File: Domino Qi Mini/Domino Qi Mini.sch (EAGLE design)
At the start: 88 parts, among them J1 MH22-1, J2 MH22-1, M1 DOMINO, Q1 AP2302GN, Q2 2SC4081, SW1 IT-1100, SW2 IT-1100, SW3 IT-1100, U1 ATMEGA32U4-XUMU, U2 MP2162GQH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

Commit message: Domino Qi Mini: work in progress
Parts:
- added U$7: DOMINO_QI_LOGO, Domino:DOMINO_QI_LOGO
- S1: value USB_MR5-003A -> USB_MR5-001; device Domino:USB_MR5-003A -> Domino:USB_MR5-001
- SW1, SW2, SW3: value IT-1100 -> IT-1210; device Domino:IT-1100 -> Domino:IT-1210; PARTNO IT-1100 -> (none)
- U1: value ATMEGA32U4-XUMU -> ATMEGA32U4-XUAU/MU; device Domino:ATMEGA32U4-XUMU -> Domino:ATMEGA32U4-XUAU/MU
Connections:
- net !RESET: now also SW1.1; no longer SW1.2
- net D+: now also D1.P$2; no longer D1.P$3
- net D-: now also D1.P$3; no longer D1.P$2
- net GND: now also SW1.2; no longer SW1.1
- net PE: now also S1.M3
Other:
- note removed: "Domino Core"
- note removed: "Domino Pi"
- note removed: "Domino Qi"
- moved on the sheet: C1, C29, R23, U1

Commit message: Work in progress: changed for PCB antenna and removed Schottky diode on Domino Qi Mini, first Domino Qi draft
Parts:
- removed D2: MBRM130LT1G, Domino:MBRM130LT1G
- A1: value ACA-5036-A2-CC-S -> RF_ANT1; device Domino:ACA-5036-A2-CC-S -> Domino:RF_ANT1
- D3, D4, D5, D6: device Domino:LED_0603 -> Domino:LED_0402
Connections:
- removed net +VUSB: D2.A, L1.1
- net !RESET: now also J1.18; no longer J1.5
- net +5V: now also L1.1; no longer D2.C
- net 3V3: now also J1.13; no longer J1.10
- net ANT0_50R: now also A1.FEED; no longer A1.A
- net AREF: now also J1.2; no longer J1.21
- net D4: now also J1.16; no longer J1.7
- net D5: now also J1.15; no longer J1.8
- net D6: now also J1.14; no longer J1.9
- net GND: now also A1.GND, J1.12; no longer A1.GND@1, A1.GND@2, J1.11
- net GP6: now also J1.3; no longer J1.20
- net HANDSHAKE: now also J1.11; no longer J1.12
- net IO10: now also J1.8; no longer J1.15
- net IO11: now also J1.7; no longer J1.16
- net IO12: now also J1.6; no longer J1.17
- net IO13: now also J1.4; no longer J1.19
- net IO8: now also J1.10; no longer J1.13
- net IO9: now also J1.9; no longer J1.14
- net RXD1: now also J1.21; no longer J1.2
- net SCL: now also J1.17; no longer J1.6
- net SDA: now also J1.19; no longer J1.4
- net TXD1: now also J1.20; no longer J1.3
- net VIN: now also J1.5; no longer J1.18

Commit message: Work in progress on Domino Qi Mini board
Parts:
- removed C2: 10u, Domino:CAP_0805
- removed C3: 100n, Domino:CAP_0402
- removed D7, D8, D9: MBRM130LT1G, Domino:MBRM130LT1G
- removed F1: 0ZCG0110FF2C, Domino:0ZCG0110FF2C
- removed L1: BLM31PG601SN1L, Domino:FB_1206
- added C32: 100n, Domino:CAP_0402
- added C33: 4u7, Domino:CAP_0805
- added C34: 10n, Domino:CAP_0402
- added L3: BLM31PG601SN1L, Domino:FB_1206
- added R26: 100k, Domino:RES_0402
- added R27: 15k, Domino:RES_0402
- added R28: 0R, Domino:RES_0402
- added U6: MP65151DJ, Domino:MP65151DJ
- R1, R2: device GeMiNi:RES_0402 -> Domino:RES_0402
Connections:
- removed net 5V: D9.C, J2.19
- removed net VPROT: F1.1, L1.2
- new net !FLAG: R28.1, U6.!FLAG
- new net EN_USB: R26.1, R28.2, U6.EN
- new net ILIM: R27.1, U6.ILIM
- net +3V3: now also J1.13; no longer D8.A
- net +5V: now also J1.5, J2.19, U6.OUT; no longer D7.C, D9.A, L1.1
- net 3V3: no longer D8.C, J1.13
- net GND: now also C32.2, C33.2, C34.2, R27.2, U6.GND; no longer C2.2, C3.2
- net VBUS: now also C34.1, L3.2; no longer C2.1, C3.1, F1.2
- net VIN: now also C32.1, C33.1, L3.1, R26.2, U6.IN; no longer D7.A, J1.5
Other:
- note added: "© 2014-2015, The Domino Team All rights reserved."
- note removed: "PolyFuse"
- note removed: "© 2014, The Domino Team All rights reserved."
- moved on the sheet: A1, C11, C12, C16, C22, C23, C24, C25, C29, C30, C31, C9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

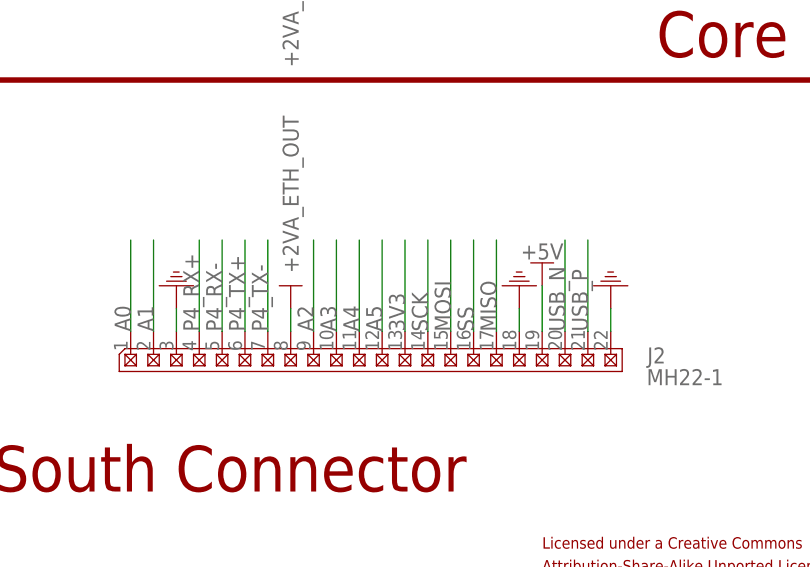
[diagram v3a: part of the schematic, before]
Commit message: Work in progress on Domino Qi Mini board: clustered all voltage translator chips instead of putting them close to ATMega32U4
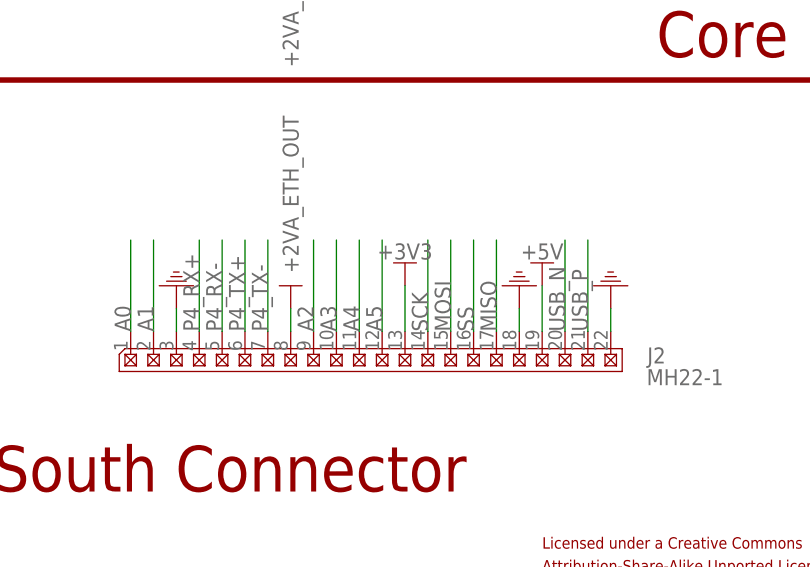
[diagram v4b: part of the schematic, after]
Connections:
- removed net 3V3: J2.13
- net +3V3: now also J2.13
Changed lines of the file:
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@@
 <?xml version="1.0" encoding="utf-8"?>
 <!DOCTYPE eagle SYSTEM "eagle.dtd">
-<eagle version="6.5.0">
+<eagle version="7.2.0">
 <drawing>
 <settings>
@@
 </part>
 <part name="SUPPLY56" library="Domino" deviceset="GND" device=""/>
+<part name="U$9" library="Domino" deviceset="+3V3" device=""/>
 </parts>
 <sheets>
@@
 </instance>
 <instance part="SUPPLY56" gate="GND" x="22.86" y="165.1" rot="MR0"/>
+<instance part="U$9" gate="G$1" x="287.02" y="50.8" smashed="yes" rot="MR0">
+<attribute name="VALUE" x="287.02" y="54.61" size="1.778" layer="96" rot="MR0" align="center"/>
+</instance>
 </instances>
 <busses>
@@
 <wire x1="284.48" y1="231.14" x2="284.48" y2="236.22" width="0.1524" layer="91"/>
 </segment>
+<segment>
+<wire x1="287.02" y1="45.72" x2="287.02" y2="50.8" width="0.1524" layer="91"/>
+<pinref part="J2" gate="G$1" pin="13"/>
+<pinref part="U$9" gate="G$1" pin="+3V3"/>
+</segment>
 </net>
 <net name="+3.3VD_IN" class="0">
@@
 </segment>
 </net>
-<net name="3V3" class="0">
-<segment>
-<wire x1="287.02" y1="45.72" x2="287.02" y2="55.88" width="0.1524" layer="91"/>
-<label x="287.02" y="45.72" size="1.778" layer="95" rot="R90"/>
-<pinref part="J2" gate="G$1" pin="13"/>
-</segment>
-</net>

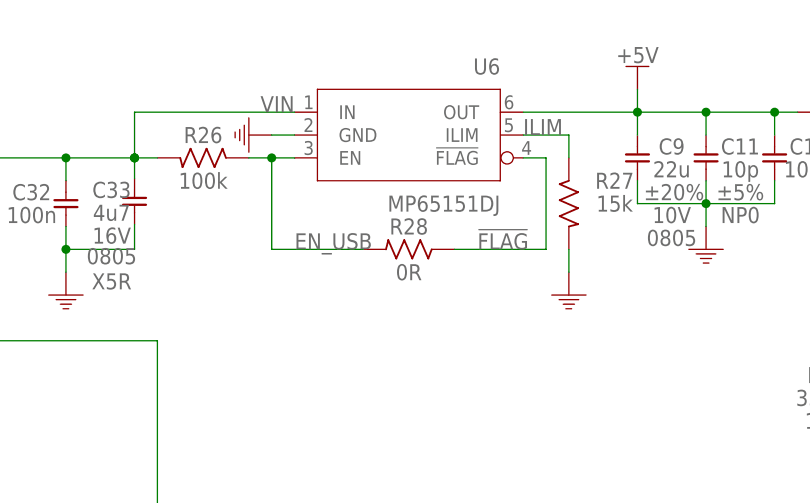
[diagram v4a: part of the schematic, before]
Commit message: Domino Qi Mini: only 1 airwire left!
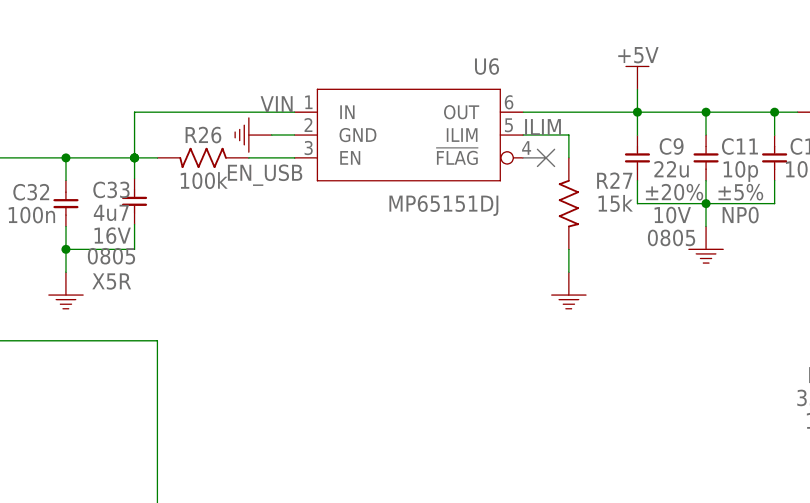
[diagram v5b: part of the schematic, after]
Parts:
- removed R28: 0R, Domino:RES_0402
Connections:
- removed net !FLAG: R28.1, U6.!FLAG
- net EN_USB: no longer R28.2
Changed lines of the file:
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@@
-<attribute name="TOL" value="5%"/>
-</part>
-<part name="R28" library="Domino" deviceset="RES_" device="0402" value="0R">
-<attribute name="PARTNO" value="R0402_0R_5%_62.5mW"/>
-<attribute name="RATE" value="62.5mW"/>
 <attribute name="TOL" value="5%"/>
 </part>
@@
 <part name="SUPPLY56" library="Domino" deviceset="GND" device=""/>
 <part name="U$9" library="Domino" deviceset="+3V3" device=""/>
+<part name="PORT3" library="Domino" deviceset="NC" device=""/>
 </parts>
 <sheets>
@@
 <attribute name="VALUE" x="73.66" y="236.22" size="1.778" layer="96" rot="MR0" align="center"/>
 </instance>
-<instance part="R28" gate="G$1" x="50.8" y="231.14" smashed="yes" rot="R180">
-<attribute name="PARTNO" x="50.8" y="231.14" size="1.778" layer="96" rot="R180" display="off"/>
-<attribute name="RATE" x="50.8" y="231.14" size="1.778" layer="96" rot="R180" display="off"/>
-<attribute name="SIZE" x="55.88" y="233.426" size="1.778" layer="96" align="center" display="off"/>
-<attribute name="TOL" x="50.8" y="231.14" size="1.778" layer="96" rot="R180" display="off"/>
-<attribute name="NAME" x="50.8" y="233.68" size="1.778" layer="95" rot="R180" align="center"/>
-<attribute name="VALUE" x="50.8" y="228.6" size="1.778" layer="96" rot="R180" align="center"/>
-</instance>
 <instance part="C34" gate="G$1" x="22.86" y="170.18" smashed="yes" rot="MR270">
 <attribute name="TC" x="22.86" y="170.18" size="1.778" layer="96" rot="MR270" display="off"/>
@@
 <attribute name="VALUE" x="287.02" y="54.61" size="1.778" layer="96" rot="MR0" align="center"/>
 </instance>
+<instance part="PORT3" gate="G$1" x="66.04" y="241.3" smashed="yes" rot="R180"/>
 </instances>
 <busses>
@@
 </segment>
 </net>
-<net name="!FLAG" class="0">
-<segment>
-<pinref part="R28" gate="G$1" pin="1"/>
-<wire x1="55.88" y1="231.14" x2="66.04" y2="231.14" width="0.1524" layer="91"/>
-<wire x1="66.04" y1="231.14" x2="66.04" y2="241.3" width="0.1524" layer="91"/>
-<pinref part="U6" gate="G$1" pin="!FLAG"/>
-<wire x1="66.04" y1="241.3" x2="63.5" y2="241.3" width="0.1524" layer="91"/>
-<label x="58.42" y="231.14" size="1.778" layer="95"/>
-</segment>
-</net>
 <net name="EN_USB" class="0">
 <segment>
-<wire x1="38.1" y1="241.3" x2="35.56" y2="241.3" width="0.1524" layer="91"/>
-<wire x1="35.56" y1="241.3" x2="33.02" y2="241.3" width="0.1524" layer="91"/>
+<label x="30.48" y="238.76" size="1.778" layer="95"/>
+<pinref part="U6" gate="G$1" pin="EN"/>
 <pinref part="R26" gate="G$1" pin="1"/>
-<pinref part="U6" gate="G$1" pin="EN"/>
-<pinref part="R28" gate="G$1" pin="2"/>
-<wire x1="45.72" y1="231.14" x2="35.56" y2="231.14" width="0.1524" layer="91"/>
-<wire x1="35.56" y1="231.14" x2="35.56" y2="241.3" width="0.1524" layer="91"/>
-<junction x="35.56" y="241.3"/>
-<label x="38.1" y="231.14" size="1.778" layer="95"/>
-</segment>
-</net>
+<wire x1="38.1" y1="241.3" x2="33.02" y2="241.3" width="0.1524" layer="91"/>
+</segment>
+</net>
